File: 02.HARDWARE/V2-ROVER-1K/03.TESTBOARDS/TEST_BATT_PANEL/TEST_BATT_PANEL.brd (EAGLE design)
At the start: 36 x 57.3 mm, 14 parts, among them J1 302-S201, Q1 PJA3416AE_R1_00001, U3 ATE1D-5M3-10-Z

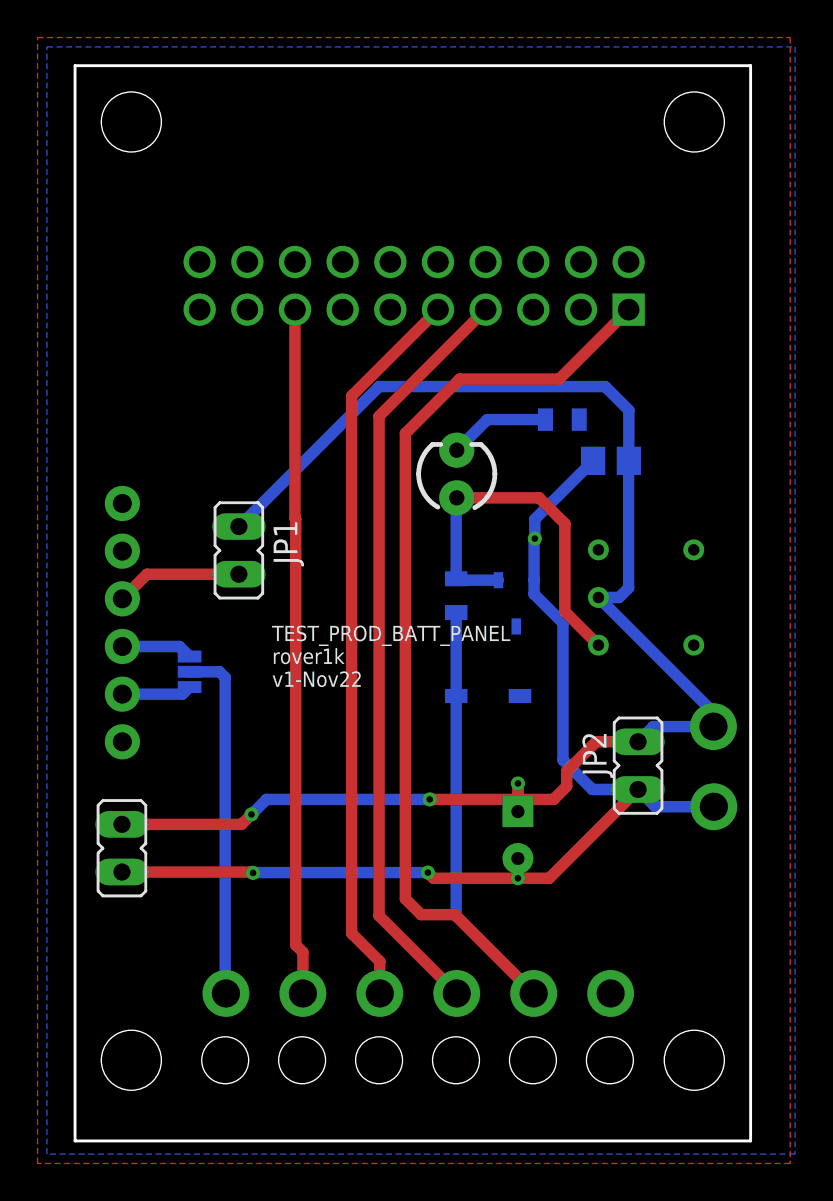
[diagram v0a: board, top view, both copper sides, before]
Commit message: Revisado y listo para pedido PCBWAY
Revision ultima antes de pedido de produccion
Modificacion de nombres
Cambio de directorio a TESTBOARDS
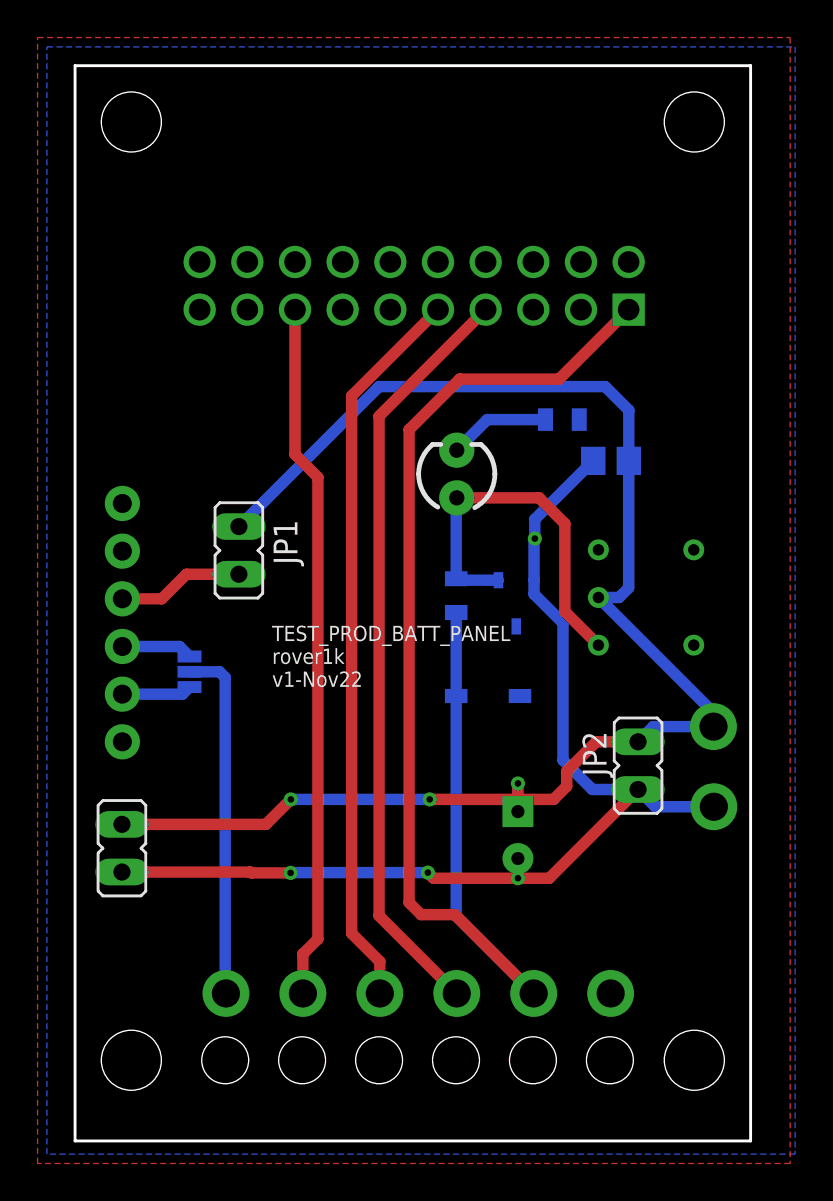
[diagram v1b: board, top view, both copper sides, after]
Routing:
- net !RESET: track 36.6 -> 37.3 mm
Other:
- board text added: "VCC de FTDI Poner SOLO cuando no este alimentado externamente"
